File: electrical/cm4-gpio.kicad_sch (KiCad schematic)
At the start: 9 parts

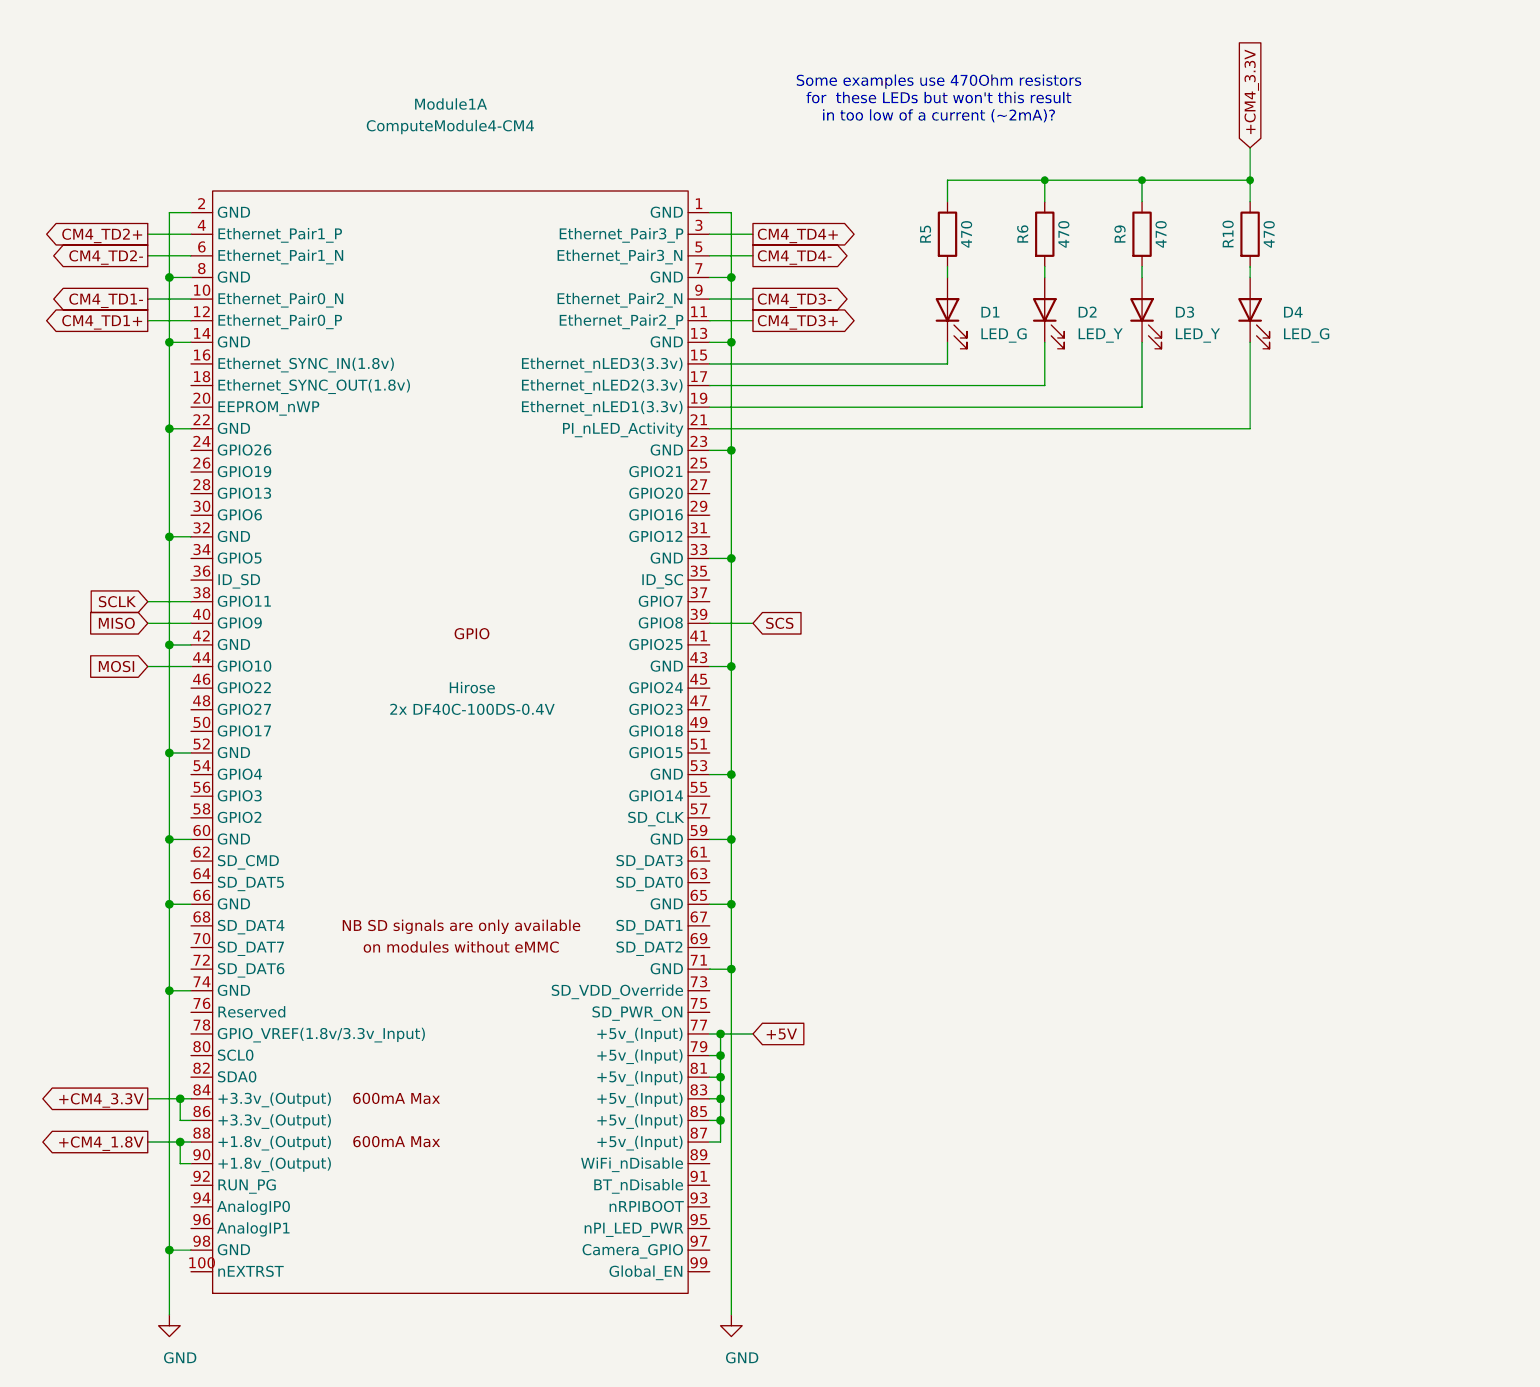
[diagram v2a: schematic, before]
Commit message: Micro B + Header for eMMC flash
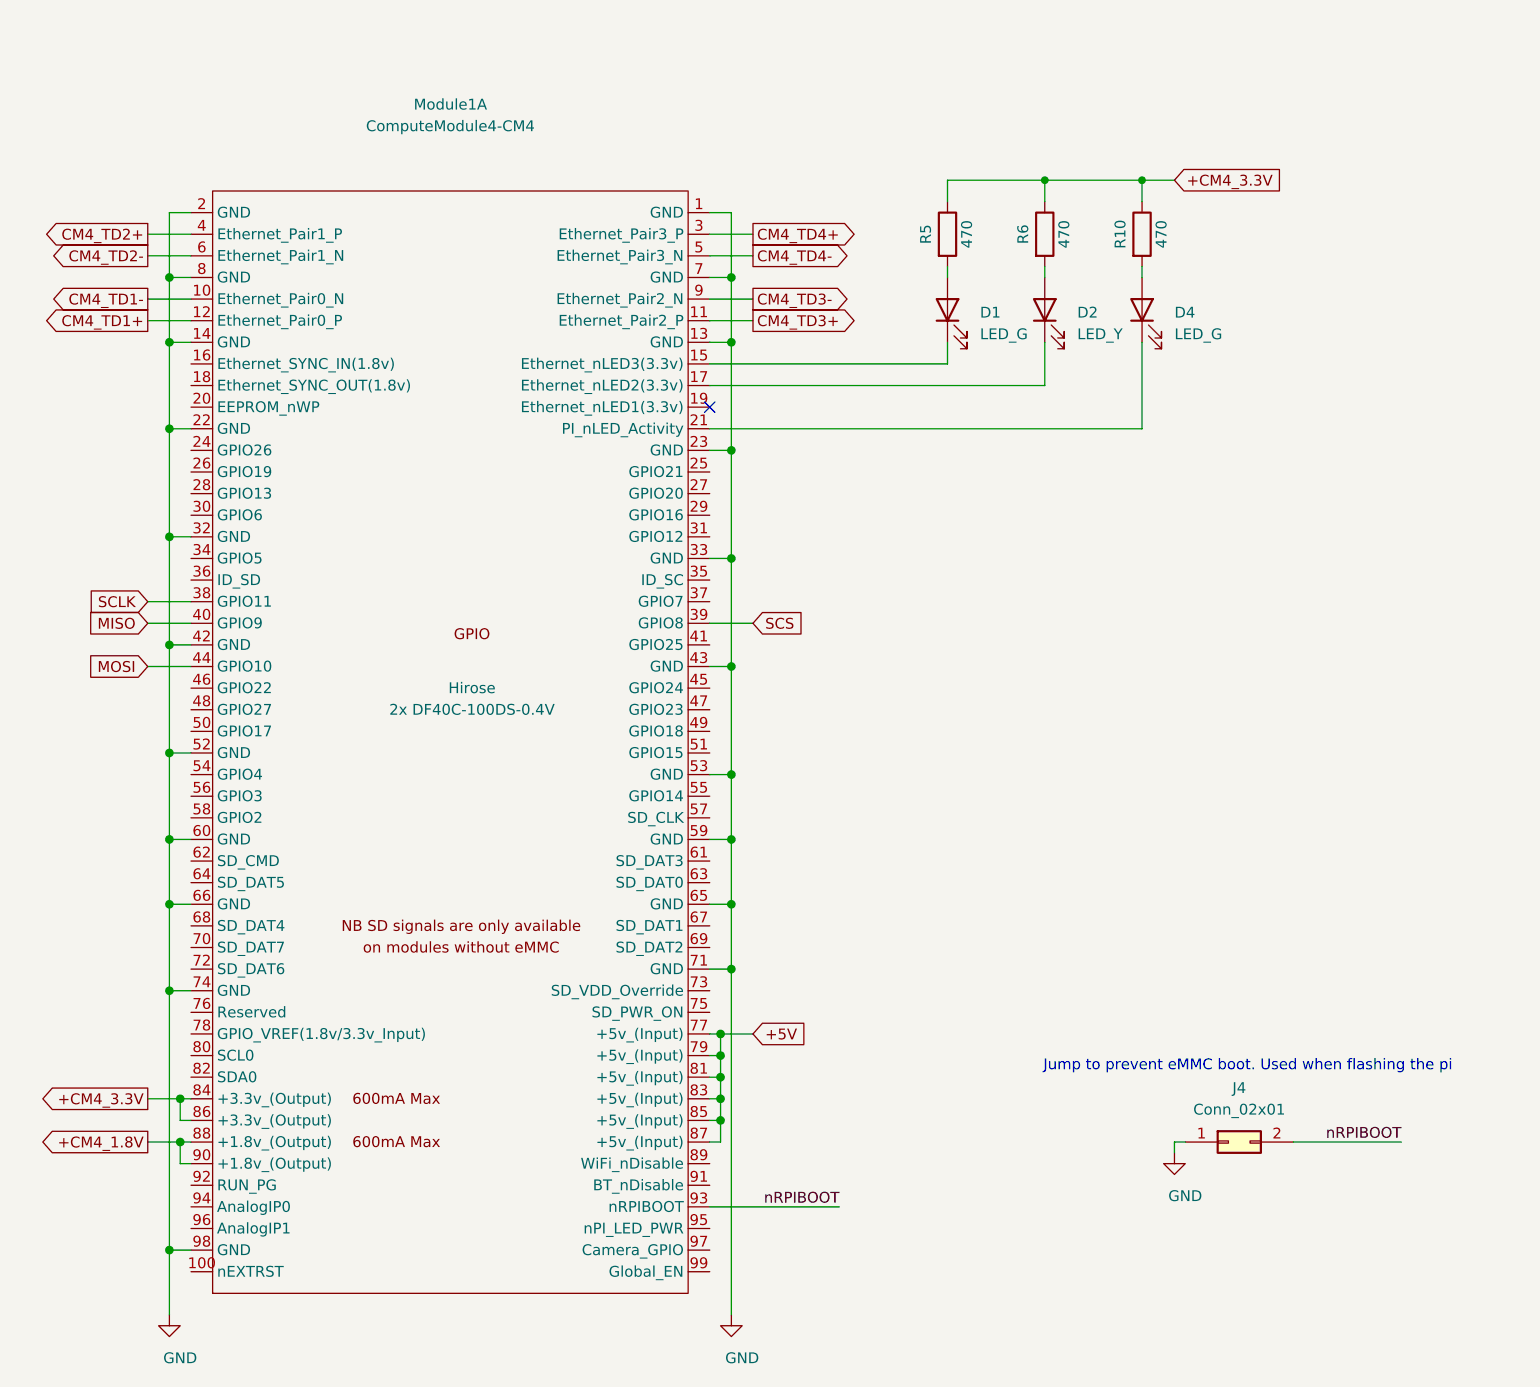
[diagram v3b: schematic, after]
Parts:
- removed D3: LED_Y, symbol Device:LED
- removed R9: 470, symbol Device:R
- added J4: Conn_02x01, symbol Connector_Generic:Conn_02x01
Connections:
- net GND: now also J4.1 (Pin_1)
- net nRPIBOOT: now reaches Module1.93 (nRPIBOOT)
- net nRPIBOOT: now also J4.2 (Pin_2)
- no-connect marks 0 -> 1
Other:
- note added: "Jump to prevent eMMC boot. Used when flashing the pi"
- note removed: "Some examples use 470Ohm resistors for these LEDs but won't this result in too low of a current (~2mA)?"
- title: Raspberry Pi Compute Module 4 Carrier Template -> Network Tap
- moved on the sheet: D4, R10
